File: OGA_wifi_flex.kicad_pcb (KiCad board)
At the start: 2 copper layers, 30 x 20 mm, 8 parts, among them J1 5034802000, U1 OGA_ESP-12E

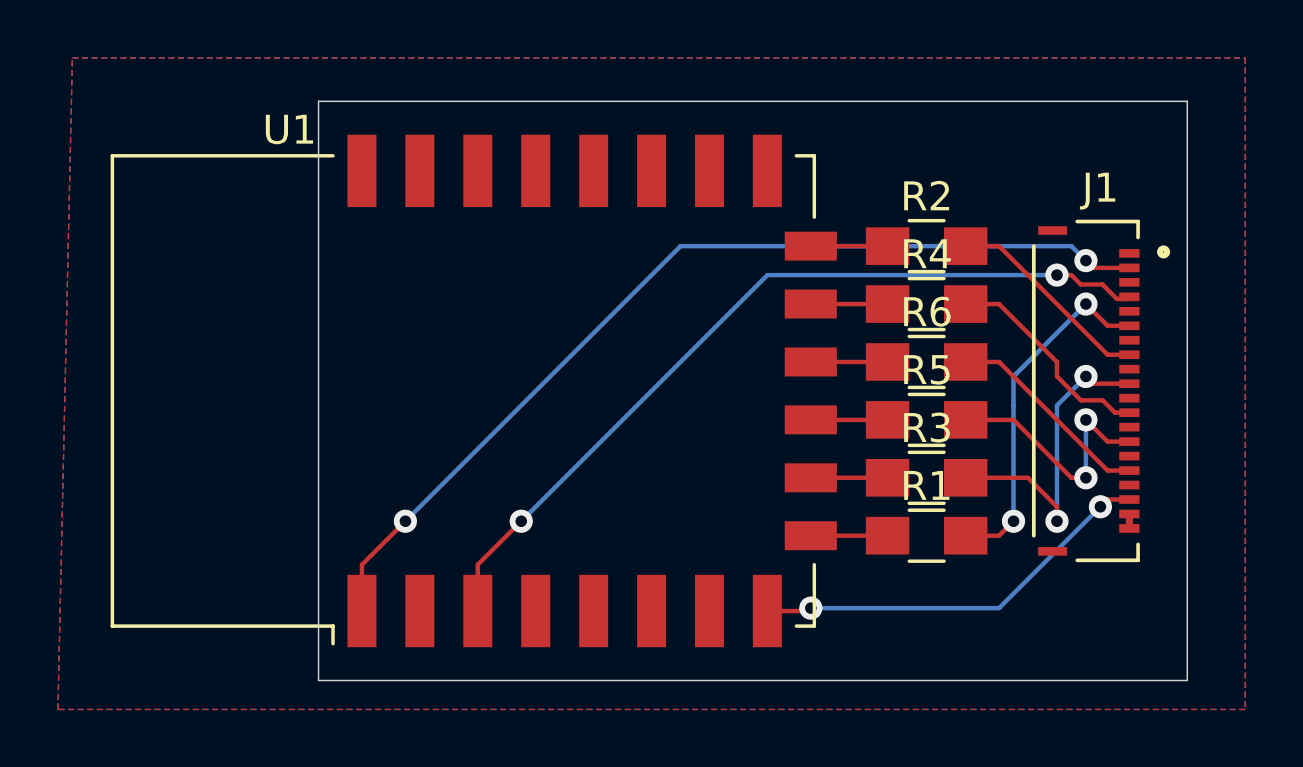
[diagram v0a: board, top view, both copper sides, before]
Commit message: different pcb and sch for this branch
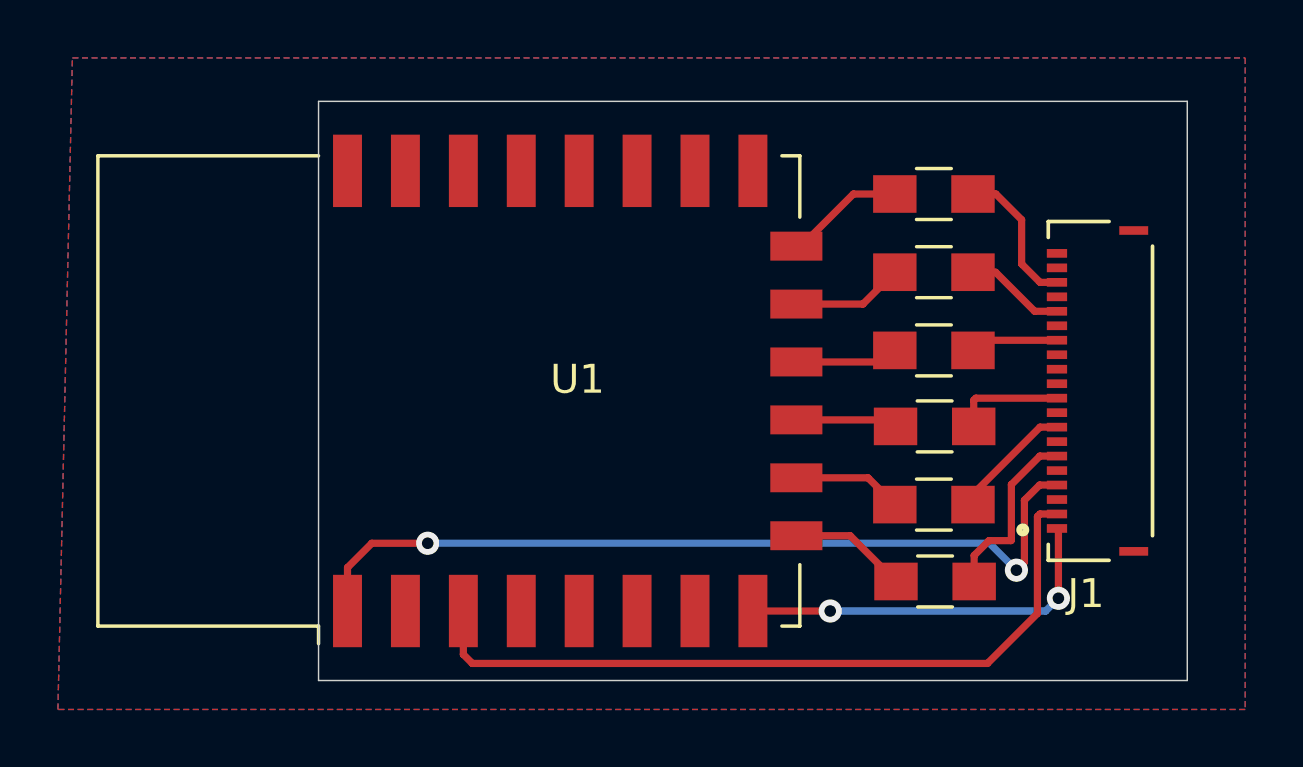
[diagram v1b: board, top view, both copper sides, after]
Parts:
- U1: value OGA_ESP-12E -> ESP-12F
- moved R2 8.93 mm to (121.2, 91.9)
- moved R6 5.81 mm to (121.2, 81.2)
- moved R5 5.11 mm to (121.2, 83.9)
- moved J1 2.50 mm to (125.5, 88.0), turned to 90 degrees
- moved R3 1.80 mm to (121.3, 89.2)
- moved R4 1.62 mm to (121.2, 86.6)
- moved R1 1.61 mm to (121.3, 94.6)
- moved U1 0.50 mm to (104.5, 88.0)
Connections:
- net Net-(J1-Pad10) renamed /sd_d2
- net Net-(J1-Pad6) renamed /sd_cmd
- net Net-(J1-Pad8) renamed /sd_d0
- J1 pad 1: GND -> VCC
- J1 pad 12: Net-(J1-Pad12) -> (no net)
- J1 pad 14: Net-(J1-Pad14) -> /sd_d3
- J1 pad 16: Net-(J1-Pad16) -> /sd_d1
- J1 pad 18: VCC -> /sd_clk
- J1 pad 2: Net-(J1-Pad2) -> /en
- J1 pad 20: GND -> (no net)
- J1 pad 4: Net-(J1-Pad4) -> /~rst
- R4 pad 2: Net-(J1-Pad12) -> /sd_d3
- R5 pad 2: Net-(J1-Pad14) -> /sd_d1
- R6 pad 2: Net-(J1-Pad16) -> /sd_clk
- U1 pad 1: Net-(J1-Pad2) -> /~rst
- U1 pad 10: Net-(R3-Pad1) -> Net-(R2-Pad1)
- U1 pad 11: Net-(R5-Pad1) -> Net-(R3-Pad1)
- U1 pad 12: Net-(R6-Pad1) -> Net-(R4-Pad1)
- U1 pad 13: Net-(R4-Pad1) -> Net-(R5-Pad1)
- U1 pad 14: Net-(R2-Pad1) -> Net-(R6-Pad1)
- U1 pad 15: Net-(U1-Pad15) -> GND
- U1 pad 16: Net-(U1-Pad16) -> (no net)
- U1 pad 17: Net-(U1-Pad17) -> (no net)
- U1 pad 18: Net-(U1-Pad18) -> (no net)
- U1 pad 19: Net-(U1-Pad19) -> (no net)
- U1 pad 2: Net-(U1-Pad2) -> (no net)
- U1 pad 20: Net-(U1-Pad20) -> (no net)
- U1 pad 21: Net-(U1-Pad21) -> (no net)
- U1 pad 22: Net-(U1-Pad22) -> (no net)
- U1 pad 3: Net-(J1-Pad4) -> /en
- U1 pad 4: Net-(U1-Pad4) -> (no net)
- U1 pad 5: Net-(U1-Pad5) -> (no net)
- U1 pad 6: Net-(U1-Pad6) -> (no net)
- U1 pad 7: Net-(U1-Pad7) -> (no net)
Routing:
- net Net-(J1-Pad2): track 33.0 -> 0.00 mm, vias 2 -> 0
- net /~rst: track 0.00 -> 29.2 mm, vias 0 -> 2
- net Net-(J1-Pad4): track 28.6 -> 0.00 mm, vias 2 -> 0
- net /en: track 0.00 -> 26.2 mm
- net Net-(J1-Pad14): track 8.79 -> 0.00 mm, vias 2 -> 0
- net Net-(J1-Pad12): track 7.50 -> 0.00 mm
- net /sd_d2: track 11.1 -> 3.81 mm, vias 2 -> 0
- net Net-(J1-Pad16): track 7.20 -> 0.00 mm
- net /sd_cmd: track 12.2 -> 6.31 mm, vias 2 -> 0
- net /sd_clk: track 0.00 -> 5.06 mm
- net /sd_d1: track 0.00 -> 3.46 mm
- net /sd_d3: track 0.00 -> 3.04 mm
- net /sd_d0: track 7.20 -> 4.22 mm
- net Net-(R6-Pad1): track 2.65 -> 4.15 mm
- net Net-(R1-Pad1): track 2.65 -> 4.09 mm
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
